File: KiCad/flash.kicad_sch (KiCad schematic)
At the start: 3 parts, among them IC4 W25Q32JWSNIQ

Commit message: Create Revision 0.0.1
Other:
- company: (none) -> ETH Zurich: Center for Project Based Learning
- title: (none) -> STDC: Flash
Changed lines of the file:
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@@
 	(generator_version "9.0")
 	(paper "A4")
+	(title_block
+		(title "STDC: Flash")
+		(date "2026-03-05")
+		(rev "0.0.1")
+		(company "ETH Zurich: Center for Project Based Learning")
+	)
 	(rectangle
 		(start 132.08 37.465)

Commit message: Added some TODOs, fixed some TODOs
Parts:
- added C60: 100n, Capacitor_SMD:C_0402_1005Metric, symbol Device:C
- renumbered R33 to R12, R34 to R33
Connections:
- net +1V8: now also C60.1
- net GND: now also C60.2
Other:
- note added: "TODO: NSS?"
- note added: "TODO: SD-Card? Memory Swap for DFU OTA"
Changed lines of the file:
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@@
 	(rectangle
 		(start 132.08 37.465)
-		(end 203.2 70.485)
+		(end 203.2 78.74)
 		(stroke
 			(width 0)
@@
 		(fill
 			(type none)
+		)
+	)
+	(text "TODO: NSS?"
+		(exclude_from_sim no)
+		(at 166.878 93.726 0)
+		(effects
+			(font
+				(size 1.27 1.27)
+			)
+		)
+	)
+	(text "TODO: SD-Card?\nMemory Swap for DFU OTA"
+		(exclude_from_sim no)
+		(at 166.878 86.868 0)
+		(effects
+			(font
+				(size 1.27 1.27)
+			)
 		)
 	)
@@
 		(color 0 0 0 0)
 	)
+	(junction
+		(at 135.89 72.39)
+		(diameter 0)
+		(color 0 0 0 0)
+	)
+	(junction
+		(at 194.31 54.61)
+		(diameter 0)
+		(color 0 0 0 0)
+	)
 	(wire
 		(pts
@@
 	(wire
 		(pts
+			(xy 135.89 73.66) (xy 135.89 72.39)
+		)
+		(stroke
+			(width 0)
+			(type default)
+		)
+	)
+	(wire
+		(pts
 			(xy 196.85 44.45) (xy 194.31 44.45)
 		)
@@
 	(wire
 		(pts
-			(xy 135.89 62.23) (xy 135.89 63.5)
-		)
-		(stroke
-			(width 0)
-			(type default)
-		)
-	)
-	(wire
-		(pts
 			(xy 135.89 43.18) (xy 135.89 44.45)
 		)
@@
 	(wire
 		(pts
+			(xy 194.31 72.39) (xy 194.31 71.12)
+		)
+		(stroke
+			(width 0)
+			(type default)
+		)
+	)
+	(wire
+		(pts
+			(xy 135.89 72.39) (xy 194.31 72.39)
+		)
+		(stroke
+			(width 0)
+			(type default)
+		)
+	)
+	(wire
+		(pts
 			(xy 137.16 59.69) (xy 135.89 59.69)
 		)
@@
 		(pts
 			(xy 132.08 54.61) (xy 137.16 54.61)
+		)
+		(stroke
+			(width 0)
+			(type default)
+		)
+	)
+	(wire
+		(pts
+			(xy 135.89 62.23) (xy 135.89 72.39)
+		)
+		(stroke
+			(width 0)
+			(type default)
+		)
+	)
+	(wire
+		(pts
+			(xy 194.31 54.61) (xy 194.31 63.5)
 		)
 		(stroke
@@
 		)
 	)
+	(hierarchical_label "SPI_NSS"
+		(shape input)
+		(at 132.08 60.96 180)
+		(effects
+			(font
+				(size 1.27 1.27)
+			)
+			(justify right)
+		)
+	)
 	(hierarchical_label "SPI_MOSI"
 		(shape input)
@@
 	(symbol
 		(lib_id "power:GND")
-		(at 135.89 63.5 0)
+		(at 135.89 73.66 0)
 		(unit 1)
 		(exclude_from_sim no)
@@
 		(on_board yes)
 		(dnp no)
-		(fields_autoplaced yes)
-		(property "Reference" "#PWR050"
-			(at 135.89 69.85 0)
+		(property "Reference" "#PWR048"
+			(at 135.89 80.01 0)
 			(effects
 				(font
@@
 		)
 		(property "Value" "GND"
-			(at 135.89 68.58 0)
+			(at 135.89 77.47 0)
 			(effects
 				(font
@@
 		)
 		(property "Footprint" ""
-			(at 135.89 63.5 0)
+			(at 135.89 73.66 0)
 			(effects
 				(font
@@
 		)
 		(property "Datasheet" ""
-			(at 135.89 63.5 0)
+			(at 135.89 73.66 0)
 			(effects
 				(font
@@
 		)
 		(property "Description" "Power symbol creates a global label with name \"GND\" , ground"
-			(at 135.89 63.5 0)
+			(at 135.89 73.66 0)
 			(effects
 				(font
@@
 		)
 		(instances
-			(project ""
-				(path "/643c756f-a801-466b-9148-7370ee6a5e00/75654986-1960-401a-97fe-a40bfa802dfa"
-					(reference "#PWR050")
+			(project "STDC"
+				(path "/643c756f-a801-466b-9148-7370ee6a5e00/a5768ca1-322e-4c77-bc87-c3070b355a8f"
+					(reference "#PWR048")
 					(unit 1)
 				)
@@
 		(on_board yes)
 		(dnp no)
-		(property "Reference" "#PWR049"
+		(property "Reference" "#PWR021"
 			(at 194.31 46.99 0)
 			(effects
@@
 		)
 		(instances
-			(project ""
-				(path "/643c756f-a801-466b-9148-7370ee6a5e00/75654986-1960-401a-97fe-a40bfa802dfa"
-					(reference "#PWR049")
+			(project "STDC"
+				(path "/643c756f-a801-466b-9148-7370ee6a5e00/a5768ca1-322e-4c77-bc87-c3070b355a8f"
+					(reference "#PWR021")
 					(unit 1)
 				)
@@
 		(on_board yes)
 		(dnp no)
-		(property "Reference" "R34"
+		(property "Reference" "R33"
 			(at 198.12 48.26 0)
 			(effects
@@
 		(instances
 			(project "STDC"
-				(path "/643c756f-a801-466b-9148-7370ee6a5e00/75654986-1960-401a-97fe-a40bfa802dfa"
-					(reference "R34")
+				(path "/643c756f-a801-466b-9148-7370ee6a5e00/a5768ca1-322e-4c77-bc87-c3070b355a8f"
+					(reference "R33")
 					(unit 1)
 				)
@@
 		(on_board yes)
 		(dnp no)
-		(property "Reference" "R33"
+		(property "Reference" "R12"
 			(at 137.16 46.99 0)
 			(effects
@@
 		)
 		(instances
-			(project ""
-				(path "/643c756f-a801-466b-9148-7370ee6a5e00/75654986-1960-401a-97fe-a40bfa802dfa"
-					(reference "R33")
+			(project "STDC"
+				(path "/643c756f-a801-466b-9148-7370ee6a5e00/a5768ca1-322e-4c77-bc87-c3070b355a8f"
+					(reference "R12")
+					(unit 1)
+				)
+			)
+		)
+	)
+	(symbol
+		(lib_id "Device:C")
+		(at 194.31 67.31 0)
+		(unit 1)
+		(exclude_from_sim no)
+		(in_bom yes)
+		(on_board yes)
+		(dnp no)
+		(property "Reference" "C60"
+			(at 196.85 66.04 0)
+			(effects
+				(font
+					(size 1.27 1.27)
+				)
+				(justify left)
+			)
+		)
+		(property "Value" "100n"
+			(at 196.85 68.58 0)
+			(effects
+				(font
+					(size 1.27 1.27)
+				)
+				(justify left)
+			)
+		)
+		(property "Footprint" "Capacitor_SMD:C_0402_1005Metric"
+			(at 195.2752 71.12 0)
+			(effects
+				(font
+					(size 1.27 1.27)
+				)
+				(hide yes)
+			)
+		)
+		(property "Datasheet" "~"
+			(at 194.31 67.31 0)
+			(effects
+				(font
+					(size 1.27 1.27)
+				)
+				(hide yes)
+			)
+		)
+		(property "Description" "Unpolarized capacitor"
+			(at 194.31 67.31 0)
+			(effects
+				(font
+					(size 1.27 1.27)
+				)
+				(hide yes)
+			)
+		)
+		(pin "2"
+		)
+		(pin "1"
+		)
+		(instances
+			(project "STDC"
+				(path "/643c756f-a801-466b-9148-7370ee6a5e00/a5768ca1-322e-4c77-bc87-c3070b355a8f"
+					(reference "C60")
 					(unit 1)
 				)
@@
 		)
 		(instances
-			(project ""
-				(path "/643c756f-a801-466b-9148-7370ee6a5e00/75654986-1960-401a-97fe-a40bfa802dfa"
+			(project "STDC"
+				(path "/643c756f-a801-466b-9148-7370ee6a5e00/a5768ca1-322e-4c77-bc87-c3070b355a8f"
 					(reference "IC4")
 					(unit 1)
@@
 		(on_board yes)
 		(dnp no)
-		(property "Reference" "#PWR048"
+		(property "Reference" "#PWR016"
 			(at 135.89 46.99 0)
 			(effects
@@
 		(instances
 			(project "STDC"
-				(path "/643c756f-a801-466b-9148-7370ee6a5e00/75654986-1960-401a-97fe-a40bfa802dfa"
-					(reference "#PWR048")
+				(path "/643c756f-a801-466b-9148-7370ee6a5e00/a5768ca1-322e-4c77-bc87-c3070b355a8f"
+					(reference "#PWR016")
 					(unit 1)
 				)

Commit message: Testing connectors, SPI2 pinout, reannotate
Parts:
- renumbered C60 to C61, R12 to R34, R33 to R35
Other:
- note removed: "TODO: NSS?"
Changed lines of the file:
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@@
-		)
-	)
-	(text "TODO: NSS?"
-		(exclude_from_sim no)
-		(at 166.878 93.726 0)
-		(effects
-			(font
-				(size 1.27 1.27)
-			)
 		)
 	)
@@
 		(shape input)
 		(at 132.08 57.15 180)
-		(effects
-			(font
-				(size 1.27 1.27)
-			)
-			(justify right)
-		)
-	)
-	(hierarchical_label "SPI_NSS"
-		(shape input)
-		(at 132.08 60.96 180)
 		(effects
 			(font
@@
 		(on_board yes)
 		(dnp no)
-		(property "Reference" "#PWR021"
+		(property "Reference" "#PWR047"
 			(at 194.31 46.99 0)
 			(effects
@@
 			(project "STDC"
 				(path "/643c756f-a801-466b-9148-7370ee6a5e00/a5768ca1-322e-4c77-bc87-c3070b355a8f"
-					(reference "#PWR021")
+					(reference "#PWR047")
 					(unit 1)
 				)
@@
 		(on_board yes)
 		(dnp no)
-		(property "Reference" "R33"
+		(property "Reference" "R35"
 			(at 198.12 48.26 0)
 			(effects
@@
 			(project "STDC"
 				(path "/643c756f-a801-466b-9148-7370ee6a5e00/a5768ca1-322e-4c77-bc87-c3070b355a8f"
-					(reference "R33")
+					(reference "R35")
 					(unit 1)
 				)
@@
 		(on_board yes)
 		(dnp no)
-		(property "Reference" "R12"
+		(property "Reference" "R34"
 			(at 137.16 46.99 0)
 			(effects
@@
 			(project "STDC"
 				(path "/643c756f-a801-466b-9148-7370ee6a5e00/a5768ca1-322e-4c77-bc87-c3070b355a8f"
-					(reference "R12")
+					(reference "R34")
 					(unit 1)
 				)
@@
 		(on_board yes)
 		(dnp no)
-		(property "Reference" "C60"
+		(property "Reference" "C61"
 			(at 196.85 66.04 0)
 			(effects
@@
 			(project "STDC"
 				(path "/643c756f-a801-466b-9148-7370ee6a5e00/a5768ca1-322e-4c77-bc87-c3070b355a8f"
-					(reference "C60")
+					(reference "C61")
 					(unit 1)
 				)
@@
 		(on_board yes)
 		(dnp no)
-		(property "Reference" "#PWR016"
+		(property "Reference" "#PWR046"
 			(at 135.89 46.99 0)
 			(effects
@@
 			(project "STDC"
 				(path "/643c756f-a801-466b-9148-7370ee6a5e00/a5768ca1-322e-4c77-bc87-c3070b355a8f"
-					(reference "#PWR016")
+					(reference "#PWR046")
 					(unit 1)
 				)

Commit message: Calculate saturation current for coils and add comments
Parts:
- renumbered C61 to C63
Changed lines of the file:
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@@
 		(on_board yes)
 		(dnp no)
-		(property "Reference" "C61"
+		(property "Reference" "C63"
 			(at 196.85 66.04 0)
 			(effects
@@
 			(project "STDC"
 				(path "/643c756f-a801-466b-9148-7370ee6a5e00/a5768ca1-322e-4c77-bc87-c3070b355a8f"
-					(reference "C61")
+					(reference "C63")
 					(unit 1)
 				)

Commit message: Add todos
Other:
- note removed: "TODO: SD-Card? Memory Swap for DFU OTA"
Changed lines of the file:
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@@
-		)
-	)
-	(text "TODO: SD-Card?\nMemory Swap for DFU OTA"
-		(exclude_from_sim no)
-		(at 166.878 86.868 0)
-		(effects
-			(font
-				(size 1.27 1.27)
-			)
 		)
 	)

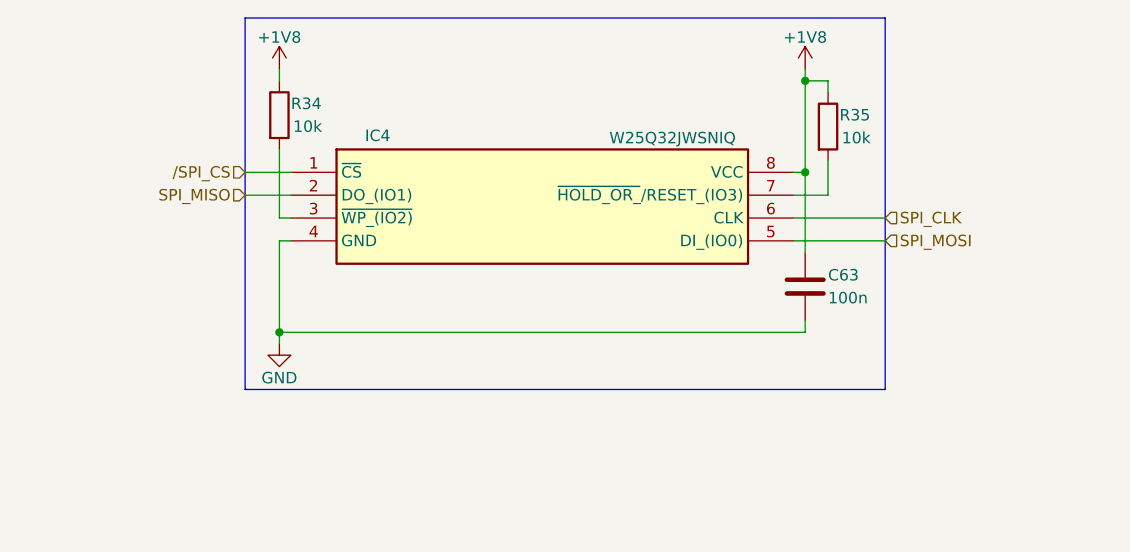
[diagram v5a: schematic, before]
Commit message: Add Pull-Down on SPI Flash Clk as per STM32 Bootloader datasheet Rev 70/page 49
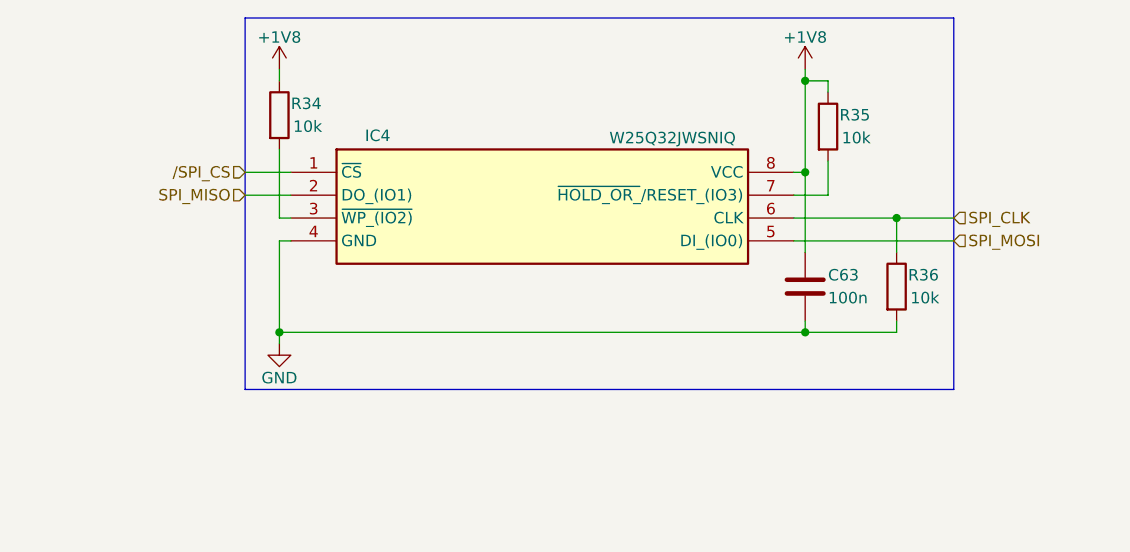
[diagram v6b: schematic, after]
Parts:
- added R36: 10k, Resistor_SMD:R_0402_1005Metric, symbol Device:R
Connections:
- net GND: now also R36.2
- net SPI_CLK: now also R36.1
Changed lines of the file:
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@@
 	(rectangle
 		(start 132.08 37.465)
-		(end 203.2 78.74)
+		(end 210.82 78.74)
 		(stroke
 			(width 0)
@@
 			(type none)
 		)
+	)
+	(junction
+		(at 204.47 59.69)
+		(diameter 0)
+		(color 0 0 0 0)
+	)
+	(junction
+		(at 194.31 72.39)
+		(diameter 0)
+		(color 0 0 0 0)
 	)
 	(junction
@@
 	(wire
 		(pts
+			(xy 204.47 71.12) (xy 204.47 72.39)
+		)
+		(stroke
+			(width 0)
+			(type default)
+		)
+	)
+	(wire
+		(pts
 			(xy 196.85 44.45) (xy 194.31 44.45)
 		)
@@
 	(wire
 		(pts
+			(xy 193.04 59.69) (xy 204.47 59.69)
+		)
+		(stroke
+			(width 0)
+			(type default)
+		)
+	)
+	(wire
+		(pts
 			(xy 193.04 54.61) (xy 194.31 54.61)
 		)
@@
 	(wire
 		(pts
-			(xy 193.04 62.23) (xy 203.2 62.23)
+			(xy 204.47 59.69) (xy 204.47 63.5)
 		)
 		(stroke
@@
 	(wire
 		(pts
-			(xy 193.04 59.69) (xy 203.2 59.69)
-		)
-		(stroke
-			(width 0)
-			(type default)
-		)
-	)
-	(wire
-		(pts
 			(xy 132.08 57.15) (xy 137.16 57.15)
 		)
@@
 		(pts
 			(xy 137.16 62.23) (xy 135.89 62.23)
+		)
+		(stroke
+			(width 0)
+			(type default)
+		)
+	)
+	(wire
+		(pts
+			(xy 204.47 59.69) (xy 210.82 59.69)
+		)
+		(stroke
+			(width 0)
+			(type default)
+		)
+	)
+	(wire
+		(pts
+			(xy 204.47 72.39) (xy 194.31 72.39)
+		)
+		(stroke
+			(width 0)
+			(type default)
+		)
+	)
+	(wire
+		(pts
+			(xy 193.04 62.23) (xy 210.82 62.23)
 		)
 		(stroke
@@
 	(hierarchical_label "SPI_CLK"
 		(shape input)
-		(at 203.2 59.69 0)
+		(at 210.82 59.69 0)
 		(effects
 			(font
@@
 	(hierarchical_label "SPI_MOSI"
 		(shape input)
-		(at 203.2 62.23 0)
+		(at 210.82 62.23 0)
 		(effects
 			(font
@@
 					(unit 1)
 				)
+			)
+		)
+	)
+	(symbol
+		(lib_id "Device:R")
+		(at 204.47 67.31 0)
+		(unit 1)
+		(exclude_from_sim no)
+		(in_bom yes)
+		(on_board yes)
+		(dnp no)
+		(property "Reference" "R36"
+			(at 205.74 66.04 0)
+			(effects
+				(font
+					(size 1.27 1.27)
+				)
+				(justify left)
+			)
+		)
+		(property "Value" "10k"
+			(at 205.994 68.58 0)
+			(effects
+				(font
+					(size 1.27 1.27)
+				)
+				(justify left)
+			)
+		)
+		(property "Footprint" "Resistor_SMD:R_0402_1005Metric"
+			(at 202.692 67.31 90)
+			(effects
+				(font
+					(size 1.27 1.27)
+				)
+				(hide yes)
+			)
+		)
+		(property "Datasheet" "~"
+			(at 204.47 67.31 0)
+			(effects
+				(font
+					(size 1.27 1.27)
+				)
+				(hide yes)
+			)
+		)
+		(property "Description" "Resistor"
+			(at 204.47 67.31 0)
+			(effects
+				(font
+					(size 1.27 1.27)
+				)
+				(hide yes)
+			)
+		)
+		(pin "2"
+		)
+		(pin "1"
+		)
+		(instances
+			(project "STDC"
+				(path "/643c756f-a801-466b-9148-7370ee6a5e00/a5768ca1-322e-4c77-bc87-c3070b355a8f"
+					(reference "R36")
+					(unit 1)
+				)

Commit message: First Draft PCB Layout
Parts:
- renumbered C63 to C60
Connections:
- net /Flash_HOLD: now reaches IC4.7 (~{HOLD_OR_}/RESET_(IO3)), R35.2
- net /Flash_WP: now reaches IC4.3 (~{WP_(IO2)}), R34.2
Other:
- moved on the sheet: R34, R35
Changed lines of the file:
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@@
 	)
 	(rectangle
-		(start 132.08 37.465)
-		(end 210.82 78.74)
+		(start 119.38 37.465)
+		(end 215.9 78.74)
 		(stroke
 			(width 0)
@@
 	(wire
 		(pts
-			(xy 193.04 57.15) (xy 196.85 57.15)
+			(xy 193.04 57.15) (xy 209.55 57.15)
 		)
 		(stroke
@@
 	(wire
 		(pts
-			(xy 196.85 44.45) (xy 194.31 44.45)
-		)
-		(stroke
-			(width 0)
-			(type default)
-		)
-	)
-	(wire
-		(pts
-			(xy 135.89 59.69) (xy 135.89 52.07)
+			(xy 209.55 44.45) (xy 194.31 44.45)
+		)
+		(stroke
+			(width 0)
+			(type default)
+		)
+	)
+	(wire
+		(pts
+			(xy 123.19 59.69) (xy 123.19 52.07)
 		)
 		(stroke
@@
 	(wire
 		(pts
-			(xy 132.08 57.15) (xy 137.16 57.15)
-		)
-		(stroke
-			(width 0)
-			(type default)
-		)
-	)
-	(wire
-		(pts
-			(xy 135.89 43.18) (xy 135.89 44.45)
+			(xy 119.38 57.15) (xy 137.16 57.15)
+		)
+		(stroke
+			(width 0)
+			(type default)
+		)
+	)
+	(wire
+		(pts
+			(xy 123.19 43.18) (xy 123.19 44.45)
 		)
 		(stroke
@@
 	(wire
 		(pts
-			(xy 137.16 59.69) (xy 135.89 59.69)
-		)
-		(stroke
-			(width 0)
-			(type default)
-		)
-	)
-	(wire
-		(pts
-			(xy 132.08 54.61) (xy 137.16 54.61)
+			(xy 137.16 59.69) (xy 123.19 59.69)
+		)
+		(stroke
+			(width 0)
+			(type default)
+		)
+	)
+	(wire
+		(pts
+			(xy 119.38 54.61) (xy 137.16 54.61)
 		)
 		(stroke
@@
 	(wire
 		(pts
-			(xy 204.47 59.69) (xy 210.82 59.69)
+			(xy 204.47 59.69) (xy 215.9 59.69)
 		)
 		(stroke
@@
 	(wire
 		(pts
-			(xy 193.04 62.23) (xy 210.82 62.23)
-		)
-		(stroke
-			(width 0)
-			(type default)
-		)
-	)
-	(wire
-		(pts
-			(xy 196.85 45.72) (xy 196.85 44.45)
-		)
-		(stroke
-			(width 0)
-			(type default)
-		)
-	)
-	(wire
-		(pts
-			(xy 196.85 57.15) (xy 196.85 53.34)
-		)
-		(stroke
-			(width 0)
-			(type default)
-		)
-	)
-	(hierarchical_label "{slash}SPI_CS"
-		(shape input)
-		(at 132.08 54.61 180)
+			(xy 193.04 62.23) (xy 215.9 62.23)
+		)
+		(stroke
+			(width 0)
+			(type default)
+		)
+	)
+	(wire
+		(pts
+			(xy 209.55 45.72) (xy 209.55 44.45)
+		)
+		(stroke
+			(width 0)
+			(type default)
+		)
+	)
+	(wire
+		(pts
+			(xy 209.55 57.15) (xy 209.55 53.34)
+		)
+		(stroke
+			(width 0)
+			(type default)
+		)
+	)
+	(label "{slash}Flash_HOLD"
+		(at 195.58 57.15 0)
 		(effects
 			(font
 				(size 1.27 1.27)
 			)
-			(justify right)
-		)
-	)
-	(hierarchical_label "SPI_CLK"
-		(shape input)
-		(at 210.82 59.69 0)
+			(justify left bottom)
+		)
+	)
+	(label "{slash}Flash_WP"
+		(at 125.73 59.69 0)
 		(effects
 			(font
 				(size 1.27 1.27)
 			)
-			(justify left)
-		)
-	)
-	(hierarchical_label "SPI_MISO"
+			(justify left bottom)
+		)
+	)
+	(hierarchical_label "{slash}SPI_CS"
 		(shape input)
-		(at 132.08 57.15 180)
+		(at 119.38 54.61 180)
 		(effects
 			(font
@@
 		)
 	)
+	(hierarchical_label "SPI_CLK"
+		(shape input)
+		(at 215.9 59.69 0)
+		(effects
+			(font
+				(size 1.27 1.27)
+			)
+			(justify left)
+		)
+	)
+	(hierarchical_label "SPI_MISO"
+		(shape input)
+		(at 119.38 57.15 180)
+		(effects
+			(font
+				(size 1.27 1.27)
+			)
+			(justify right)
+		)
+	)
 	(hierarchical_label "SPI_MOSI"
 		(shape input)
-		(at 210.82 62.23 0)
+		(at 215.9 62.23 0)
 		(effects
 			(font
@@
 		(on_board yes)
 		(dnp no)
-		(property "Reference" "#PWR048"
+		(property "Reference" "#PWR045"
 			(at 135.89 80.01 0)
 			(effects
@@
 			(project "STDC"
 				(path "/643c756f-a801-466b-9148-7370ee6a5e00/a5768ca1-322e-4c77-bc87-c3070b355a8f"
-					(reference "#PWR048")
+					(reference "#PWR045")
 					(unit 1)
 				)
@@
 		(on_board yes)
 		(dnp no)
-		(property "Reference" "#PWR047"
+		(property "Reference" "#PWR044"
 			(at 194.31 46.99 0)
 			(effects
@@
 			(project "STDC"
 				(path "/643c756f-a801-466b-9148-7370ee6a5e00/a5768ca1-322e-4c77-bc87-c3070b355a8f"
-					(reference "#PWR047")
+					(reference "#PWR044")
 					(unit 1)
 				)
@@
 	(symbol
 		(lib_id "Device:R")
-		(at 196.85 49.53 0)
+		(at 209.55 49.53 0)
 		(unit 1)
 		(exclude_from_sim no)
@@
 		(dnp no)
 		(property "Reference" "R35"
-			(at 198.12 48.26 0)
+			(at 210.82 48.26 0)
 			(effects
 				(font
@@
 		)
 		(property "Value" "10k"
-			(at 198.374 50.8 0)
+			(at 211.074 50.8 0)
 			(effects
 				(font
@@
 		)
 		(property "Footprint" "Resistor_SMD:R_0402_1005Metric"
-			(at 195.072 49.53 90)
+			(at 207.772 49.53 90)
 			(effects
 				(font
@@
 		)
 		(property "Datasheet" "~"
-			(at 196.85 49.53 0)
+			(at 209.55 49.53 0)
 			(effects
 				(font
@@
 		)
 		(property "Description" "Resistor"
-			(at 196.85 49.53 0)
+			(at 209.55 49.53 0)
 			(effects
 				(font
@@
 	(symbol
 		(lib_id "Device:R")
-		(at 135.89 48.26 0)
+		(at 123.19 48.26 0)
 		(unit 1)
 		(exclude_from_sim no)
@@
 		(dnp no)
 		(property "Reference" "R34"
-			(at 137.16 46.99 0)
+			(at 124.46 46.99 0)
 			(effects
 				(font
@@
 		)
 		(property "Value" "10k"
-			(at 137.414 49.53 0)
+			(at 124.714 49.53 0)
 			(effects
 				(font
@@
 		)
 		(property "Footprint" "Resistor_SMD:R_0402_1005Metric"
-			(at 134.112 48.26 90)
+			(at 121.412 48.26 90)
 			(effects
 				(font
@@
 		)
 		(property "Datasheet" "~"
-			(at 135.89 48.26 0)
+			(at 123.19 48.26 0)
 			(effects
 				(font
@@
 		)
 		(property "Description" "Resistor"
-			(at 135.89 48.26 0)
+			(at 123.19 48.26 0)
 			(effects
 				(font
@@
 		(on_board yes)
 		(dnp no)
-		(property "Reference" "C63"
+		(property "Reference" "C60"
 			(at 196.85 66.04 0)
 			(effects
@@
 			(project "STDC"
 				(path "/643c756f-a801-466b-9148-7370ee6a5e00/a5768ca1-322e-4c77-bc87-c3070b355a8f"
-					(reference "C63")
+					(reference "C60")
 					(unit 1)
 				)
@@
 	(symbol
 		(lib_id "power:+1V8")
-		(at 135.89 43.18 0)
+		(at 123.19 43.18 0)
 		(unit 1)
 		(exclude_from_sim no)
@@
 		(on_board yes)
 		(dnp no)
-		(property "Reference" "#PWR046"
-			(at 135.89 46.99 0)
+		(property "Reference" "#PWR043"
+			(at 123.19 46.99 0)
 			(effects
 				(font
@@
 		)
 		(property "Value" "+1V8"
-			(at 135.89 39.624 0)
+			(at 123.19 39.624 0)
 			(effects
 				(font
@@
 		)
 		(property "Footprint" ""
-			(at 135.89 43.18 0)
+			(at 123.19 43.18 0)
 			(effects
 				(font
@@
 		)
 		(property "Datasheet" ""
-			(at 135.89 43.18 0)
+			(at 123.19 43.18 0)
 			(effects
 				(font
@@
 		)
 		(property "Description" "Power symbol creates a global label with name \"+1V8\""
-			(at 135.89 43.18 0)
+			(at 123.19 43.18 0)
 			(effects
 				(font
@@
 			(project "STDC"
 				(path "/643c756f-a801-466b-9148-7370ee6a5e00/a5768ca1-322e-4c77-bc87-c3070b355a8f"
-					(reference "#PWR046")
+					(reference "#PWR043")
 					(unit 1)
 				)
